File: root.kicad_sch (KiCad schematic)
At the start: 2 parts, among them J3 SIM8060-6-1-14-00-A, U1 BG95-M3

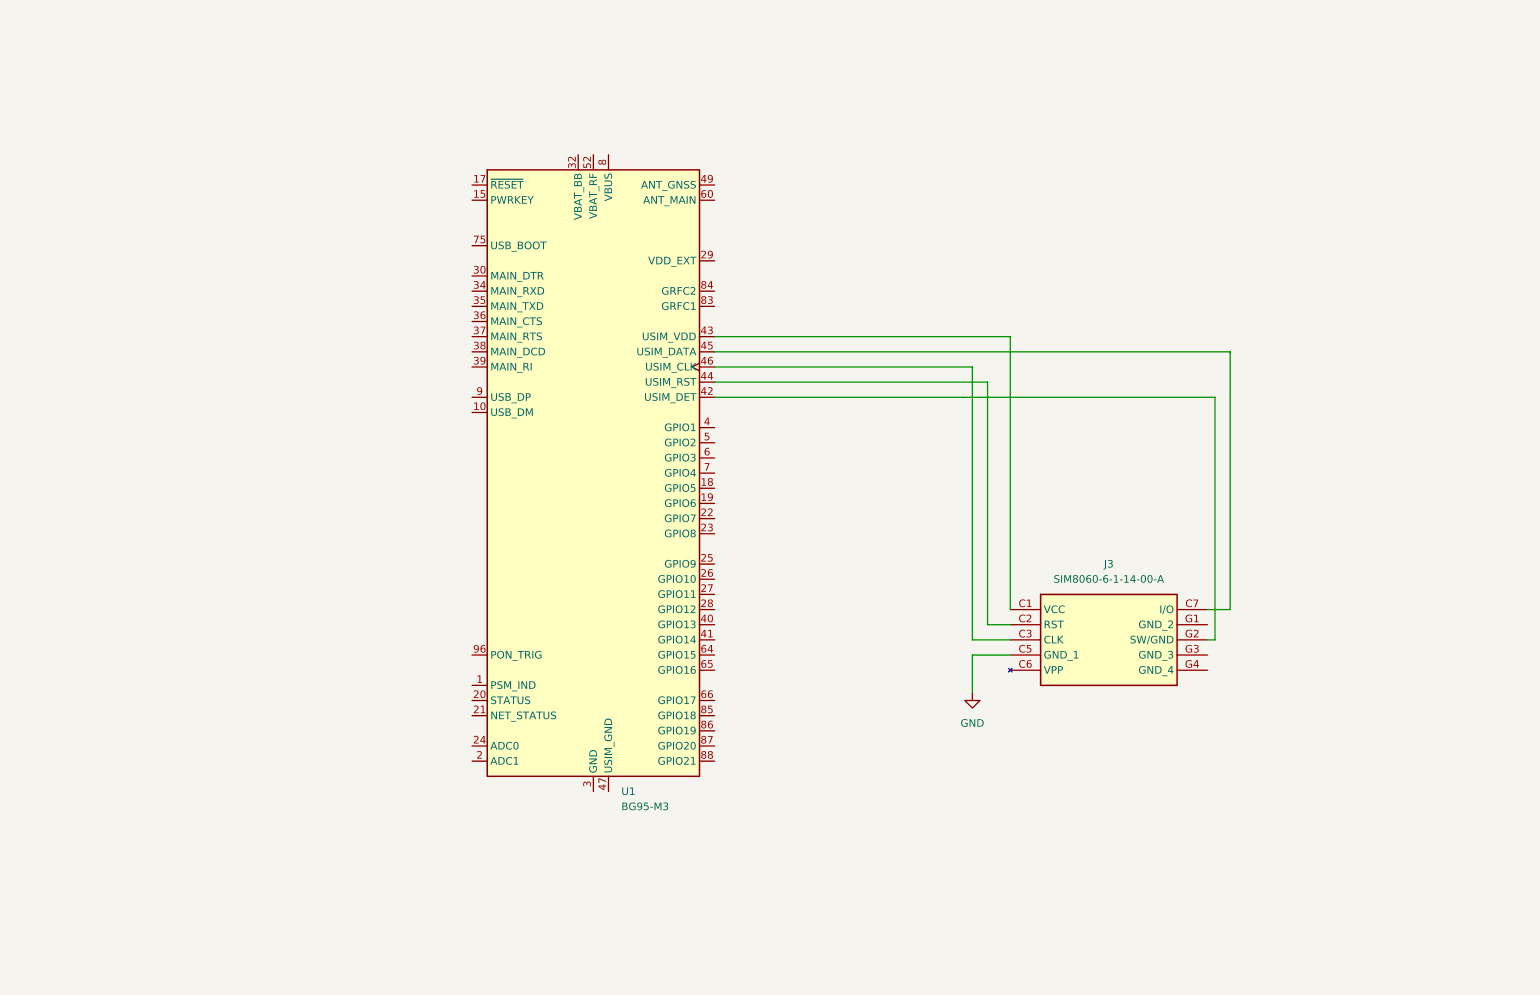
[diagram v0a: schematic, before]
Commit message: Add project library symbols and KiCad updates
This change updates the KiCad project to use the Project_Parts symbol library and refreshes the tracker schematic symbol metadata. It adds the SN74AXC4T245 level shifter, BG95 modem and SIM connector references, and associated decoupling/ground net connections. The patch also restores the ESP32-C6 and ASM330 symbols to the current design and registers the new project symbol library in sym-lib-table.
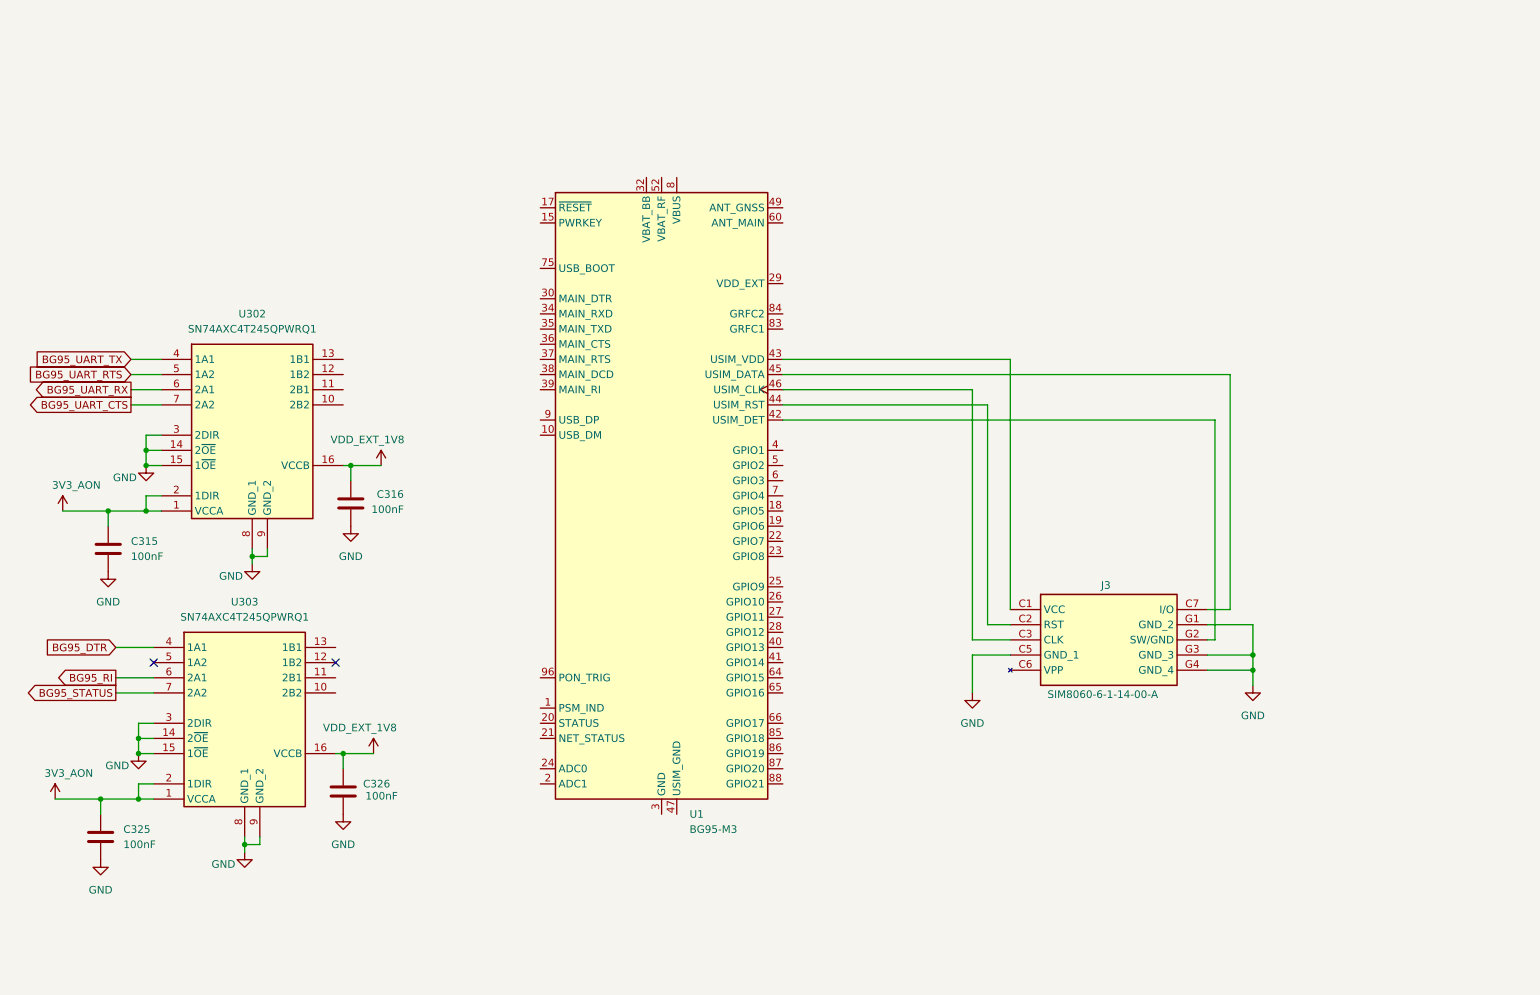
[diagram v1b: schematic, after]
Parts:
- added C315, C316, C325, C326: 100nF, RF_Module:ESP32-C6-MINI-1, symbol Device:C
- added U302: SN74AXC4T245QPWRQ1, SOP65P640X120-16N, symbol SamacSys_Parts:SN74AXC4T245QPWRQ1
- added U303: SN74AXC4T245QPWRQ1, SOP65P640X120-16N, symbol Project_Parts:SN74AXC4T245QPWRQ1
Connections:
- net GND: now also J3.G1 (GND_2), J3.G3 (GND_3), J3.G4 (GND_4), C315.2, C316.2, C325.2, C326.2, U302.14 (2~{OE}), U302.15 (1~{OE}), U302.3 (2DIR), U302.8 (GND_1), U302.9 (GND_2), U303.14 (2~{OE}), U303.15 (1~{OE}), U303.3 (2DIR), U303.8 (GND_1), U303.9 (GND_2)
- new net 3V3_AON: C315.1, C325.1, U302.1 (VCCA), U302.2 (1DIR), U303.1 (VCCA), U303.2 (1DIR)
- new net BG95_DTR: U303.4 (1A1)
- new net BG95_RI: U303.6 (2A1)
- new net BG95_STATUS: U303.7 (2A2)
- new net BG95_UART_CTS: U302.7 (2A2)
- new net BG95_UART_RTS: U302.5 (1A2)
- new net BG95_UART_RX: U302.6 (2A1)
- new net BG95_UART_TX: U302.4 (1A1)
- new net VDD_EXT_1V8: C316.1, C326.1, U302.16 (VCCB), U303.16 (VCCB)
- no-connect marks 0 -> 2
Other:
- moved on the sheet: U1

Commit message: Update KiCad schematic parts and positions
Update schematic and project files: adjust used_designators in Tracker.kicad_pro; add/modify many symbols in root.kicad_sch (Device:R resistors, SamacSys MMBT3904 transistors, power GND/VCC symbols, and device instances). Update BG95 component properties and pin coordinates, replace SIM8060 symbol entries with MMBT3904 where appropriate, add/rename resistors (R303–R306) and multiple global labels (BG95 signals). Numerous footprint, datasheet and wiring/junction coordinate adjustments to reflect component replacements and repositioning.
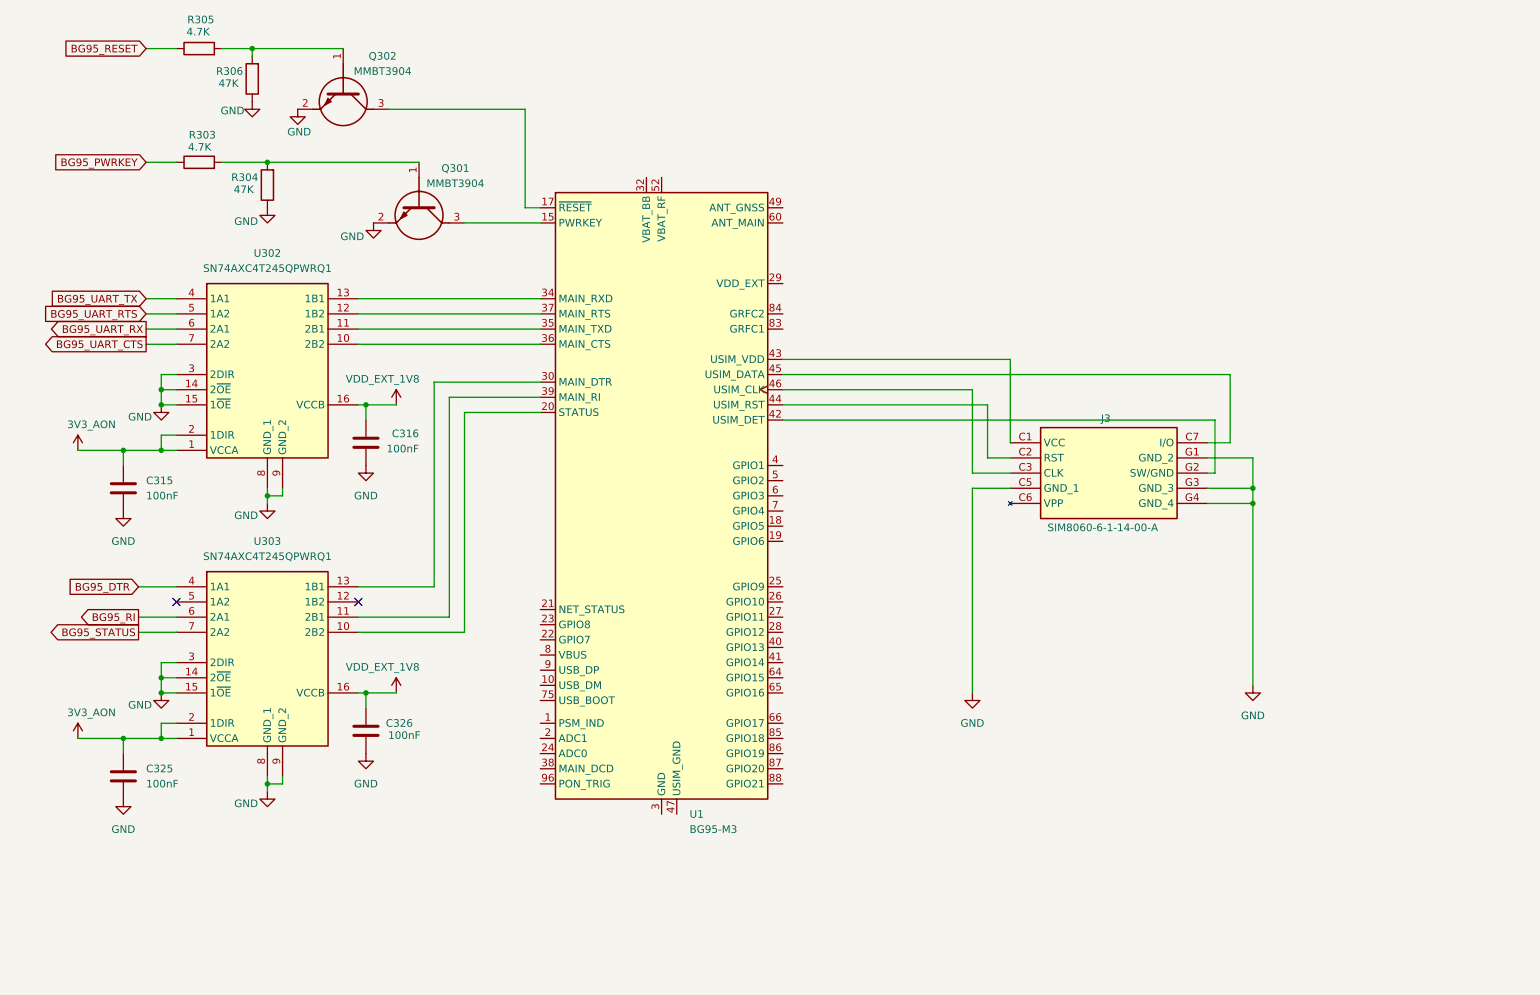
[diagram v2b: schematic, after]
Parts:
- added Q301, Q302: MMBT3904, SOT95P230X110-3N, symbol SamacSys_Parts:MMBT3904
- added R303, R305: 4.7K, symbol Device:R
- added R304, R306: 47K, symbol Device:R
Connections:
- net GND: now also Q301.2 (E), Q302.2 (E), R304.1, R306.1
- net at U303.10 (2B2): now also U1.20 (STATUS)
- net at U303.11 (2B1): now also U1.39 (MAIN_RI)
- net at U303.13 (1B1): now also U1.30 (MAIN_DTR)
- net at U1.15 (PWRKEY): now also Q301.3 (C)
- net at U1.17 (~{RESET}): now also Q302.3 (C)
- net at U1.34 (MAIN_RXD): now also U302.13 (1B1)
- net at U1.35 (MAIN_TXD): now also U302.11 (2B1)
- net at U1.36 (MAIN_CTS): now also U302.10 (2B2)
- net at U1.37 (MAIN_RTS): now also U302.12 (1B2)
- new net: Q301.1 (B), R303.2, R304.2
- new net: Q302.1 (B), R305.2, R306.2
- new net BG95_PWRKEY: R303.1
- new net BG95_RESET: R305.1
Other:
- moved on the sheet: C315, C316, C325, C326, J3, U302, U303

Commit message: Update BG95 interface and SIM protection
This schematic update adds the missing BG95 UART/SIM protection and test-point instrumentation, including ESD diodes, pull resistors, and updated voltage-translation circuitry. It also refreshes the KiCad designator inventory to match the newly added components and symbols on the tracker board.
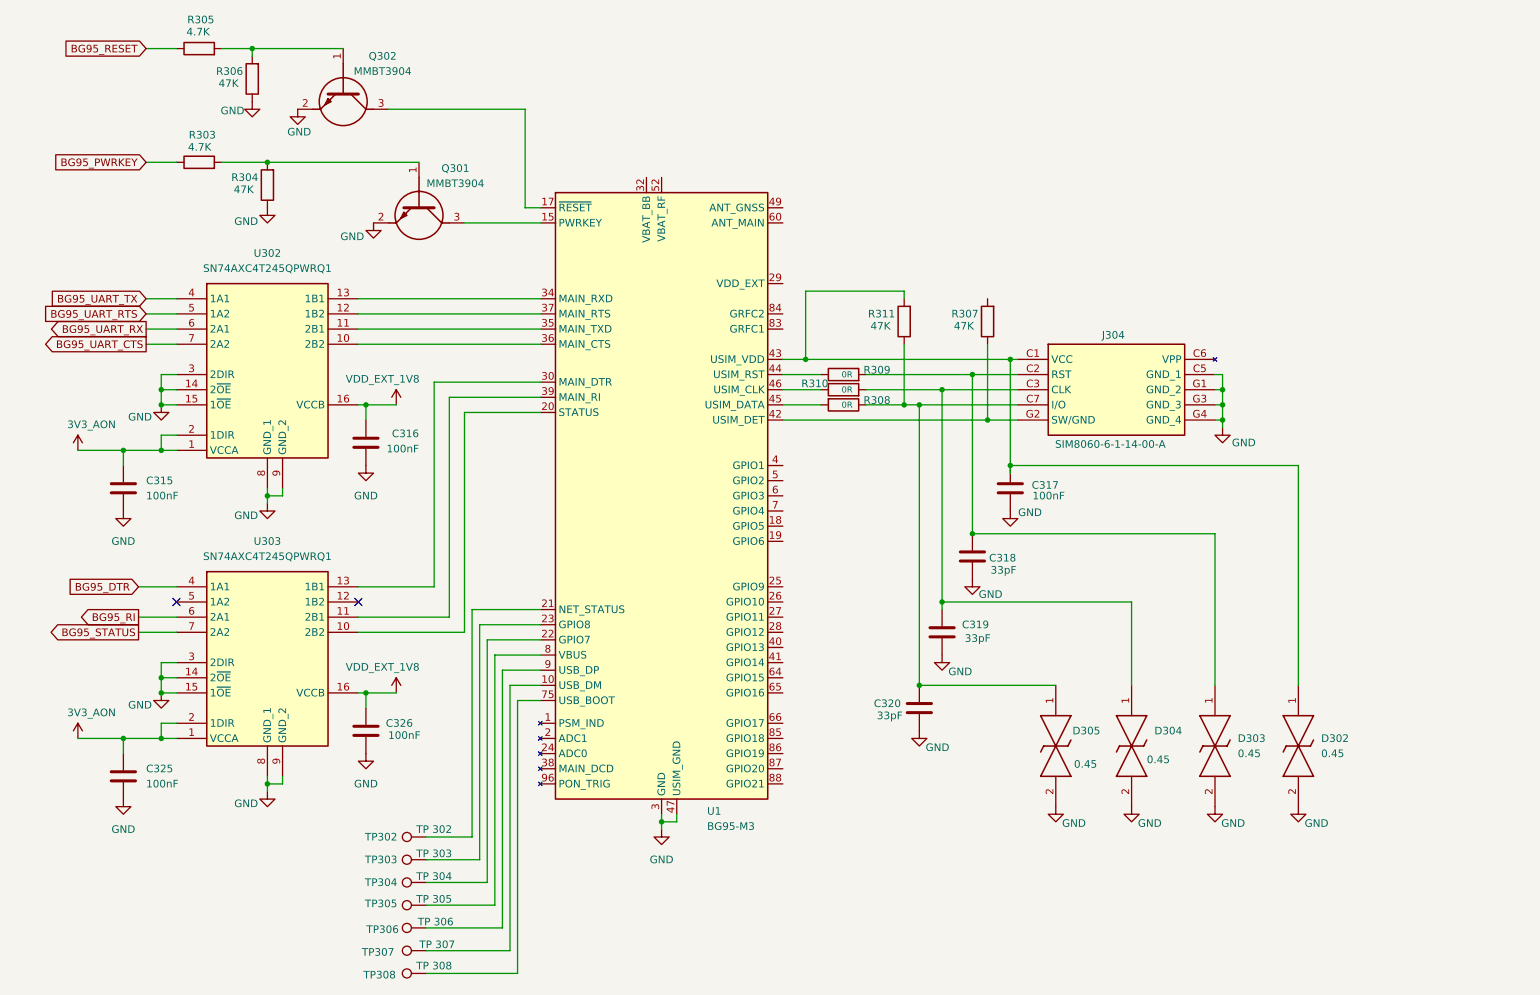
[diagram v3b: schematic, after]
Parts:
- added C317: 100nF, RF_Module:ESP32-C6-MINI-1, symbol Device:C
- added C318, C319, C320: 33pF, RF_Module:ESP32-C6-MINI-1, symbol Device:C
- added D302, D303, D304, D305: TPD1E10B06DPYR, SamacSys_Parts:TPD1E10B06DPYR, symbol SamacSys_Parts:TPD1E10B06DPYR
- added R307, R311: 47K, symbol Device:R
- added R308, R309, R310: 0R, symbol Device:R
- added TP302: TP 302, SOT95P230X110-3N, symbol Connector:TestPoint
- added TP303: TP 303, SOT95P230X110-3N, symbol Connector:TestPoint
- added TP304: TP 304, SOT95P230X110-3N, symbol Connector:TestPoint
- added TP305: TP 305, SOT95P230X110-3N, symbol Connector:TestPoint
- added TP306: TP 306, SOT95P230X110-3N, symbol Connector:TestPoint
- added TP307: TP 307, SOT95P230X110-3N, symbol Connector:TestPoint
- added TP308: TP 308, SOT95P230X110-3N, symbol Connector:TestPoint
- renumbered J3 to J304
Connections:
- net GND: now also U1.100 (GND), U1.101 (GND), U1.102 (GND), U1.3 (GND), U1.31 (GND), U1.47 (USIM_GND), U1.48 (GND), U1.50 (GND), U1.54 (GND), U1.55 (GND), U1.58 (GND), U1.59 (GND), U1.61 (GND), U1.62 (GND), U1.67 (GND), U1.68 (GND), U1.69 (GND), U1.70 (GND), U1.71 (GND), U1.72 (GND), U1.73 (GND), U1.74 (GND), U1.79 (GND), U1.80 (GND), U1.81 (GND), U1.82 (GND), U1.89 (GND), U1.90 (GND), U1.91 (GND), C317.2, C318.1, C319.2, C320.1, D302.2, D303.2, D304.2, D305.2
- net at J304.C1 (VCC), U1.43 (USIM_VDD): now also C317.1, D302.1, R311.2
- net at J304.C2 (RST): now also C318.2, D303.1, R309.2; no longer U1.44 (USIM_RST)
- net at U1.46 (USIM_CLK): now also R310.1; no longer J304.C3 (CLK)
- net at J304.C7 (I/O): now also C320.2, D305.1, R308.1, R311.1; no longer U1.45 (USIM_DATA)
- net at J304.G2 (SW/GND), U1.42 (USIM_DET): now also R307.1
- net at U1.10 (USB_DM): now also TP307.1
- net at U1.21 (NET_STATUS): now also TP302.1
- net at U1.22 (GPIO7): now also TP304.1
- net at U1.23 (GPIO8): now also TP303.1
- net at U1.75 (USB_BOOT): now also TP308.1
- net at U1.8 (VBUS): now also TP305.1
- net at U1.9 (USB_DP): now also TP306.1
- new net: C319.1, D304.1, J304.C3 (CLK), R310.2
- new net: R308.2, U1.45 (USIM_DATA)
- new net: R309.1, U1.44 (USIM_RST)
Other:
- moved on the sheet: J304

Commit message: Update BG95 schematic and power nets
This commit revises the tracker schematic to match the updated BG95 and power-distribution design. It adds missing power flags and net labels, updates component references and footprints, adds coaxial and connector symbols, and swaps several passives/ferrite beads to better reflect the final BOM. The netlist is also cleaned up by renaming references and correcting no-connect/power pin assignments so the KiCad project remains consistent and ERC-friendly.
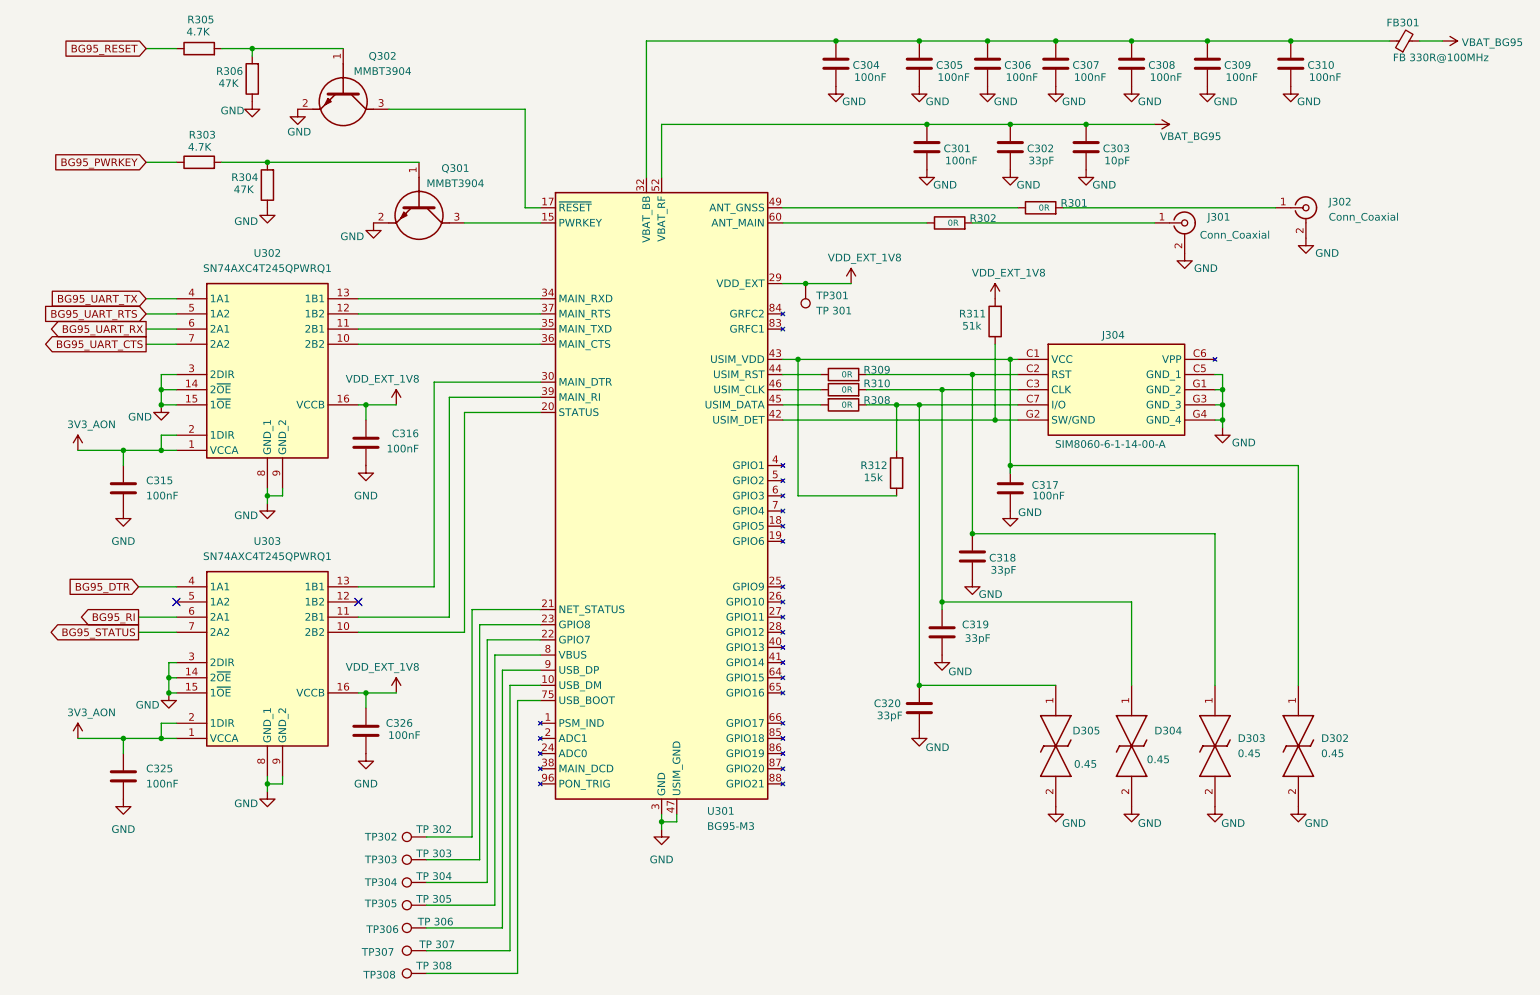
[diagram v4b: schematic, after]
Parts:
- removed R311: 47K, symbol Device:R
- added C301, C304, C305, C306, C307, C308, C309, C310: 100nF, RF_Module:ESP32-C6-MINI-1, symbol Device:C
- added C302: 33pF, RF_Module:ESP32-C6-MINI-1, symbol Device:C
- added C303: 10pF, RF_Module:ESP32-C6-MINI-1, symbol Device:C
- added FB301: FB 330R@100MHz, symbol Device:FerriteBead_Small
- added J301, J302: Conn_Coaxial, symbol Connector:Conn_Coaxial
- added R301, R302: 0R, symbol Device:R
- added R312: 15k, symbol Device:R
- added TP301: TP 301, SOT95P230X110-3N, symbol Connector:TestPoint
- R311: renamed from R307; value 47K -> 51k
- renumbered U1 to U301
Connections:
- net GND: now also C301.1, C302.1, C303.1, C304.1, C305.1, C306.1, C307.1, C308.1, C309.1, C310.1, J301.2 (Ext), J302.2 (Ext)
- net VDD_EXT_1V8: now also R311.2, U301.29 (VDD_EXT), TP301.1
- net at C320.2, D305.1, J304.C7 (I/O)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: now also R312.2
- net at C317.1, D302.1, J304.C1 (VCC)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: now also R312.1
- net at U301.32 (VBAT_BB), U301.33 (VBAT_BB): now also C304.2, C305.2, C306.2, C307.2, C308.2, C309.2, C310.2, FB301.1
- net at U301.49 (ANT_GNSS): now also R301.1
- net VBAT_BG95: now reaches U301.52 (VBAT_RF), U301.53 (VBAT_RF)
- net VBAT_BG95: now also C301.2, C302.2, C303.2, FB301.2
- net at U301.60 (ANT_MAIN): now also R302.1
- new net: J301.1 (In), R302.2
- new net: J302.1 (In), R301.2
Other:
- moved on the sheet: R311
